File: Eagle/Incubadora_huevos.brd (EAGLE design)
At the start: 100 x 80 mm, 40 parts, among them K1 G5L, K2 G5L, Q1 2N3904, Q2 2N3904, U1 SHT20

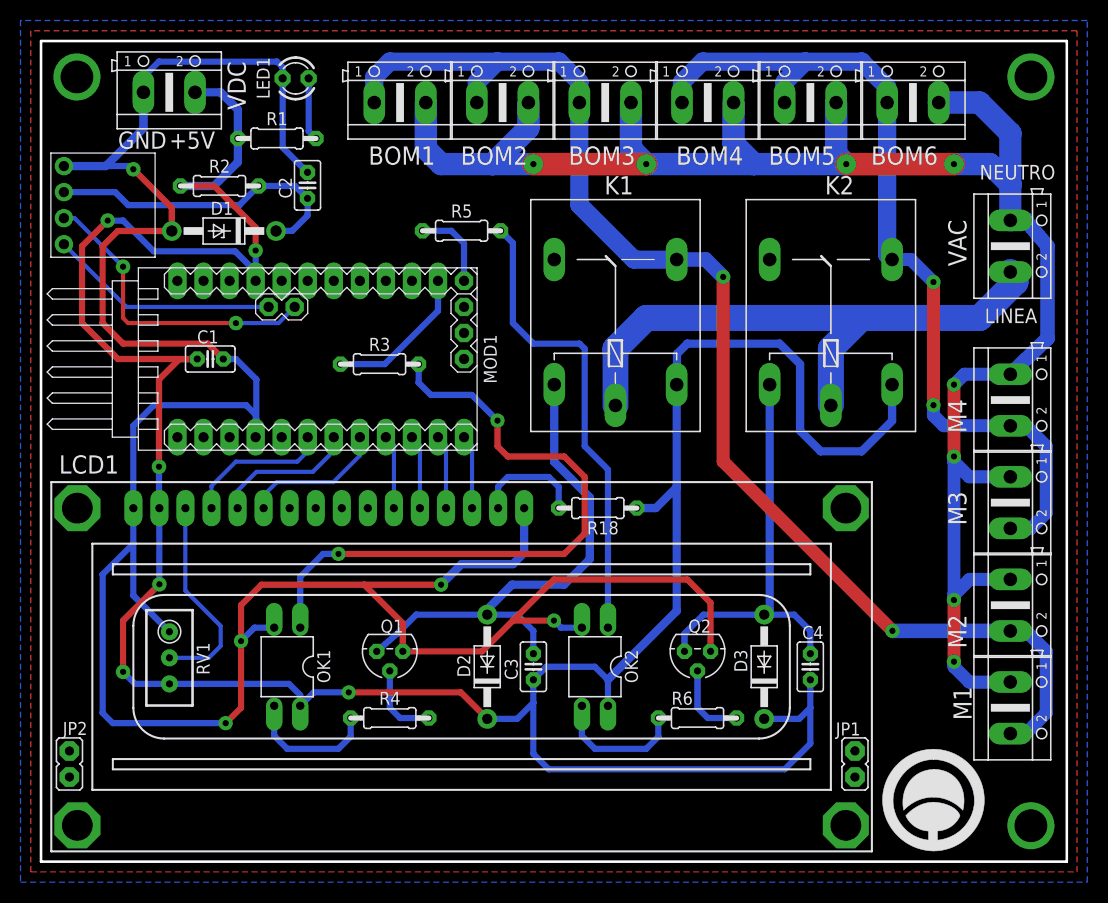
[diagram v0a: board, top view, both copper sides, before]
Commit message: Se agrego resistencias pull up a la PCB
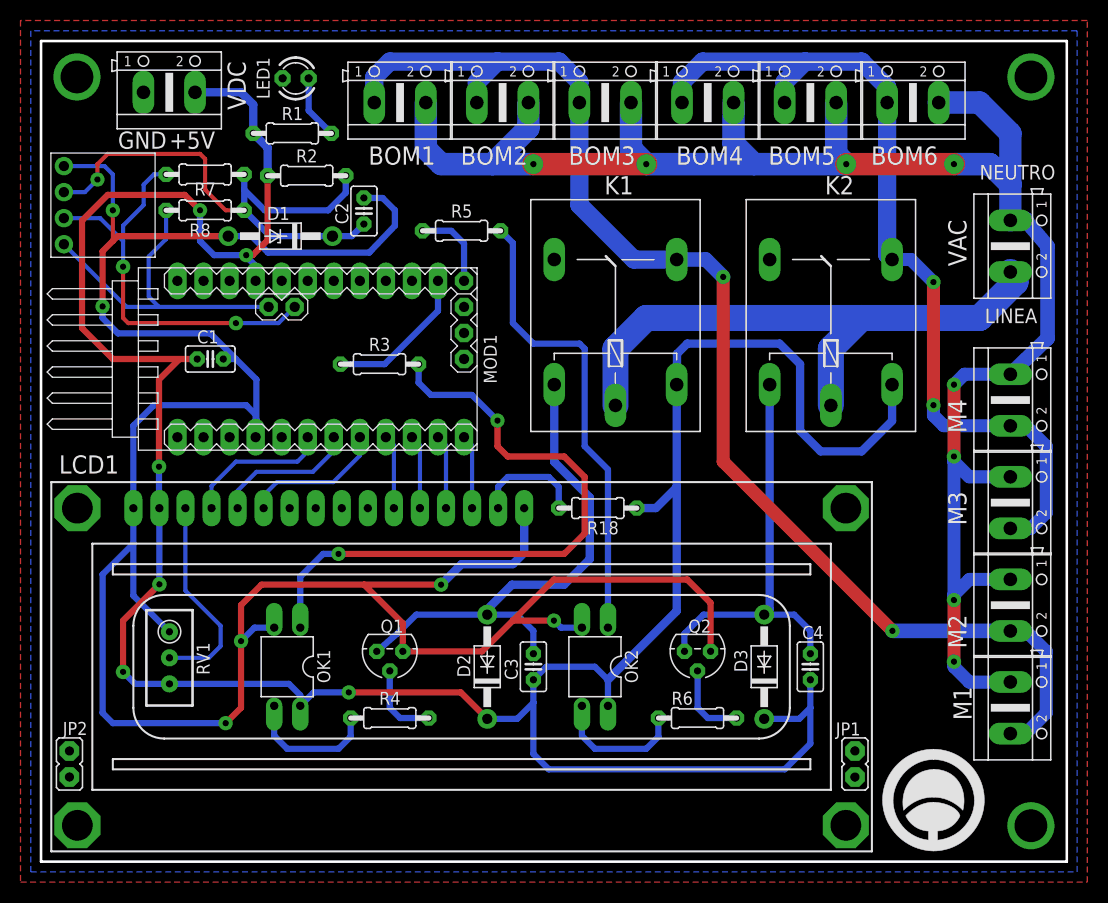
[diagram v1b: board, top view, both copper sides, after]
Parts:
- added R7, R8: 4k7, rcl:0204/7
- moved R2 8.56 mm to (25.9, 66.9)
- moved C2 6.04 mm to (31.5, 63.4)
- moved D1 5.52 mm to (23.3, 61.0)
- moved R1 1.58 mm to (24.5, 71.0)
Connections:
- net +3V3: now also R7.1, R8.1
- net SCL: now also R8.2
- net SDA: now also R7.2
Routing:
- net +3V3: track 30.9 -> 53.8 mm, vias 0 -> 1
- net GND: track 261.7 -> 247.4 mm, vias 5 -> 6
- net SCL: track 22.5 -> 33.0 mm
- net SDA: track 30.3 -> 40.7 mm
- net +5V: track 281.8 -> 278.8 mm
